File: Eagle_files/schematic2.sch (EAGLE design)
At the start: 76 parts, among them IC6 DS3231/SO

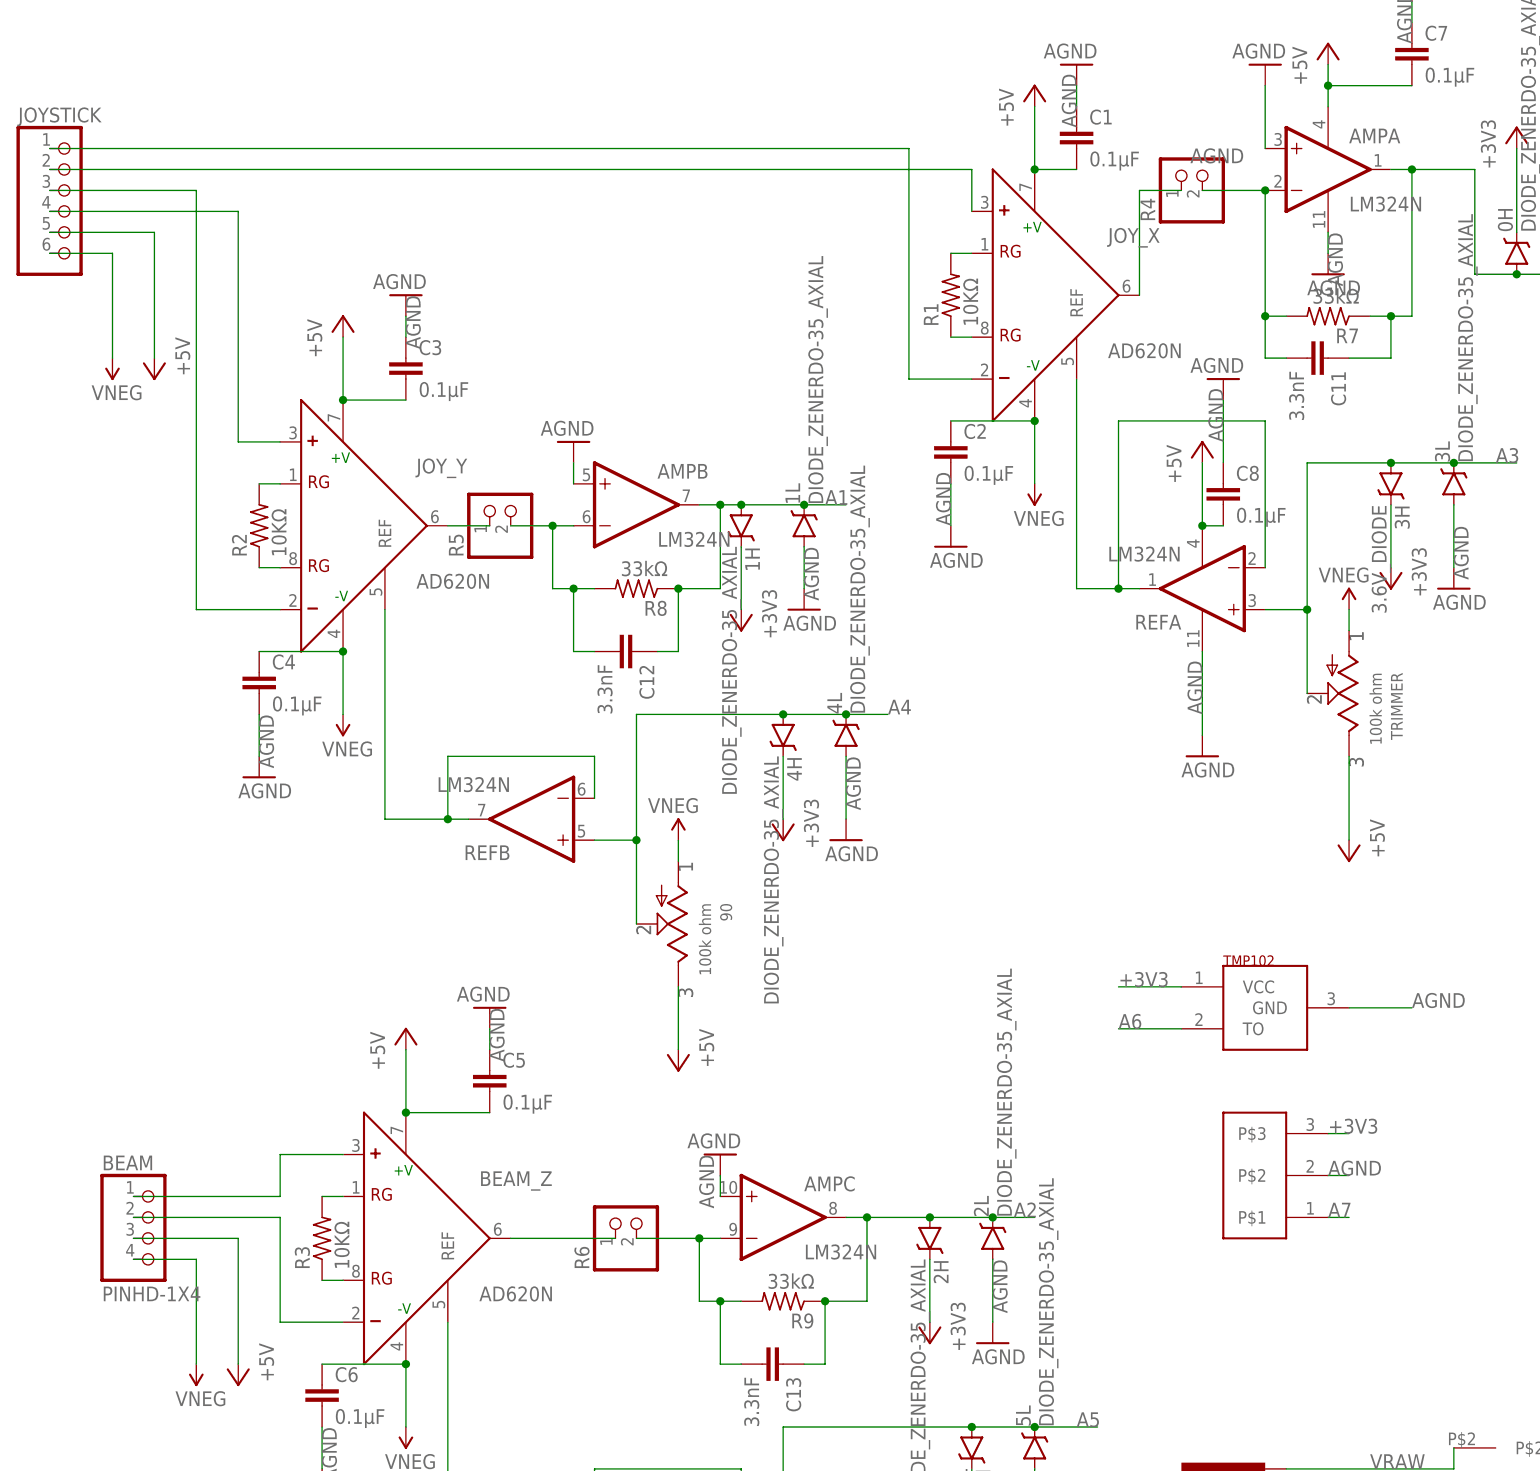
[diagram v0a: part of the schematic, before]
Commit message: Aligned all of the diodes to make a little more room. Increased the spacing between the analog ground plane and the neighboring planes. Rewired the A7 analog header so it conforms to standard TMP35, LM35 style temperature sensor pinouts. Swapped the gain-setting resistors on the In-AMPS to 2-pin header style so that we can swap resistors easily to change gain.
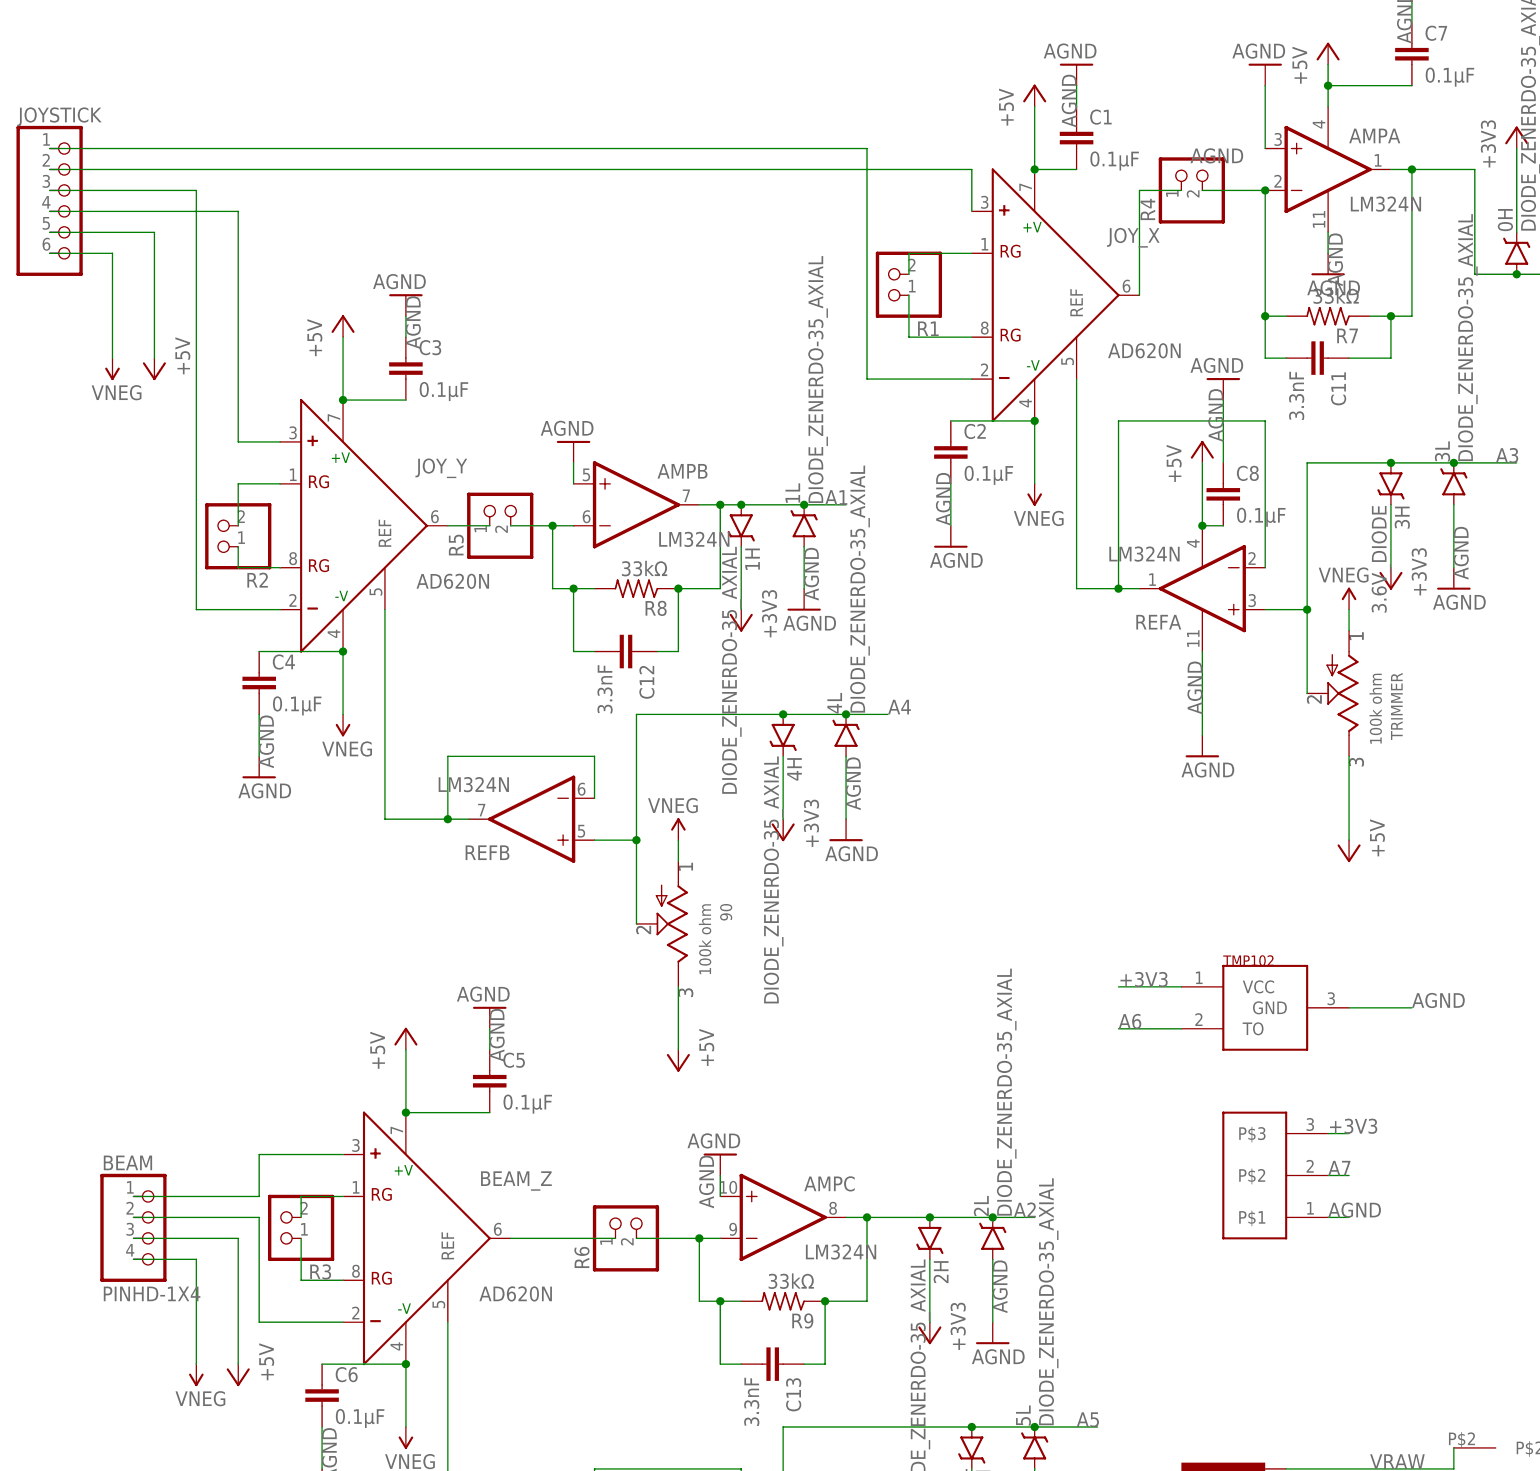
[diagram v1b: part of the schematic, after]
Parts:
- R1, R2, R3: value 10KΩ -> (none); device Felicia_force_logger:RESISTOR_SMDR0805 -> Felicia_force_logger:PINHD-1X2
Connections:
- net A7: now also ANALOG7_HEADER.P$2; no longer ANALOG7_HEADER.P$1
- net AGND: now also ANALOG7_HEADER.P$1; no longer ANALOG7_HEADER.P$2
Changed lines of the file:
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@@
 <part name="C12" library="Felicia_force_logger" deviceset="CAP" device="0805" value="3.3nF"/>
 <part name="C11" library="Felicia_force_logger" deviceset="CAP" device="0805" value="3.3nF"/>
-<part name="R2" library="Felicia_force_logger" deviceset="RESISTOR_SMD" device="R0805" value="10KΩ"/>
-<part name="R1" library="Felicia_force_logger" deviceset="RESISTOR_SMD" device="R0805" value="10KΩ"/>
-<part name="R3" library="Felicia_force_logger" deviceset="RESISTOR_SMD" device="R0805" value="10KΩ"/>
 <part name="U$3" library="Felicia_force_logger" deviceset="DC-DC_CONVERTER_DUAL_SUPPLY" device=""/>
 <part name="GND7" library="Felicia_force_logger" deviceset="GND" device=""/>
@@
 <part name="STANDOFF2" library="miller" deviceset="STAND-OFF" device=""/>
 <part name="I2C_HEADER" library="Felicia_force_logger" deviceset="PINHD-1X6" device="LOCK"/>
+<part name="R2" library="Felicia_force_logger" deviceset="PINHD-1X2" device=""/>
+<part name="R1" library="Felicia_force_logger" deviceset="PINHD-1X2" device=""/>
+<part name="R3" library="Felicia_force_logger" deviceset="PINHD-1X2" device=""/>
 </parts>
 <sheets>
@@
 <instance part="C12" gate="G$1" x="66.04" y="139.7" rot="R270"/>
 <instance part="C11" gate="G$1" x="149.86" y="175.26" rot="R270"/>
-<instance part="R2" gate="G$1" x="22.86" y="154.94" rot="R90"/>
-<instance part="R1" gate="G$1" x="106.68" y="182.88" rot="R90"/>
-<instance part="R3" gate="G$1" x="30.48" y="68.58" rot="R90"/>
 <instance part="U$3" gate="G$1" x="170.18" y="15.24"/>
 <instance part="GND7" gate="1" x="147.32" y="7.62"/>
@@
 <instance part="STANDOFF2" gate="G$1" x="12.7" y="5.08"/>
 <instance part="I2C_HEADER" gate="A" x="314.96" y="160.02"/>
+<instance part="R2" gate="G$1" x="17.78" y="154.94" rot="R180"/>
+<instance part="R1" gate="G$1" x="99.06" y="185.42" rot="R180"/>
+<instance part="R3" gate="G$1" x="25.4" y="71.12" rot="R180"/>
 </instances>
 <busses>
@@
 <segment>
 <pinref part="JOY_X" gate="G$1" pin="RG@1"/>
-<wire x1="106.68" y1="187.96" x2="109.22" y2="187.96" width="0.1524" layer="91"/>
 <pinref part="R1" gate="G$1" pin="2"/>
+<wire x1="109.22" y1="187.96" x2="101.6" y2="187.96" width="0.1524" layer="91"/>
+<wire x1="101.6" y1="187.96" x2="101.6" y2="185.42" width="0.1524" layer="91"/>
 </segment>
 </net>
@@
 <segment>
 <pinref part="JOY_X" gate="G$1" pin="RG@2"/>
-<wire x1="106.68" y1="177.8" x2="109.22" y2="177.8" width="0.1524" layer="91"/>
 <pinref part="R1" gate="G$1" pin="1"/>
+<wire x1="109.22" y1="177.8" x2="101.6" y2="177.8" width="0.1524" layer="91"/>
+<wire x1="101.6" y1="177.8" x2="101.6" y2="182.88" width="0.1524" layer="91"/>
 </segment>
 </net>
@@
 <segment>
 <pinref part="BEAM_Z" gate="G$1" pin="RG@1"/>
-<wire x1="30.48" y1="73.66" x2="33.02" y2="73.66" width="0.1524" layer="91"/>
 <pinref part="R3" gate="G$1" pin="2"/>
+<wire x1="33.02" y1="73.66" x2="27.94" y2="73.66" width="0.1524" layer="91"/>
+<wire x1="27.94" y1="73.66" x2="27.94" y2="71.12" width="0.1524" layer="91"/>
 </segment>
 </net>
@@
 <segment>
 <pinref part="BEAM_Z" gate="G$1" pin="RG@2"/>
-<wire x1="30.48" y1="63.5" x2="33.02" y2="63.5" width="0.1524" layer="91"/>
 <pinref part="R3" gate="G$1" pin="1"/>
+<wire x1="33.02" y1="63.5" x2="27.94" y2="63.5" width="0.1524" layer="91"/>
+<wire x1="27.94" y1="63.5" x2="27.94" y2="68.58" width="0.1524" layer="91"/>
 </segment>
 </net>
@@
 <net name="N$19" class="0">
 <segment>
-<wire x1="101.6" y1="200.66" x2="101.6" y2="172.72" width="0.1524" layer="91"/>
+<wire x1="96.52" y1="200.66" x2="96.52" y2="172.72" width="0.1524" layer="91"/>
 <pinref part="JOY_X" gate="G$1" pin="-"/>
-<wire x1="101.6" y1="172.72" x2="109.22" y2="172.72" width="0.1524" layer="91"/>
+<wire x1="96.52" y1="172.72" x2="109.22" y2="172.72" width="0.1524" layer="91"/>
 <pinref part="JOYSTICK" gate="A" pin="1"/>
-<wire x1="-2.54" y1="200.66" x2="101.6" y2="200.66" width="0.1524" layer="91"/>
+<wire x1="-2.54" y1="200.66" x2="96.52" y2="200.66" width="0.1524" layer="91"/>
 </segment>
 </net>
@@
 <pinref part="JOY_Y" gate="G$1" pin="RG@1"/>
 <pinref part="R2" gate="G$1" pin="2"/>
-<wire x1="22.86" y1="160.02" x2="25.4" y2="160.02" width="0.1524" layer="91"/>
+<wire x1="25.4" y1="160.02" x2="20.32" y2="160.02" width="0.1524" layer="91"/>
+<wire x1="20.32" y1="160.02" x2="20.32" y2="154.94" width="0.1524" layer="91"/>
 </segment>
 </net>
@@
 <pinref part="JOY_Y" gate="G$1" pin="RG@2"/>
 <pinref part="R2" gate="G$1" pin="1"/>
-<wire x1="22.86" y1="149.86" x2="25.4" y2="149.86" width="0.1524" layer="91"/>
+<wire x1="25.4" y1="149.86" x2="20.32" y2="149.86" width="0.1524" layer="91"/>
+<wire x1="20.32" y1="149.86" x2="20.32" y2="152.4" width="0.1524" layer="91"/>
 </segment>
 </net>
@@
 <segment>
 <pinref part="BEAM" gate="G$1" pin="2"/>
-<wire x1="7.62" y1="71.12" x2="25.4" y2="71.12" width="0.1524" layer="91"/>
-<wire x1="25.4" y1="71.12" x2="25.4" y2="58.42" width="0.1524" layer="91"/>
+<wire x1="7.62" y1="71.12" x2="22.86" y2="71.12" width="0.1524" layer="91"/>
+<wire x1="22.86" y1="71.12" x2="22.86" y2="58.42" width="0.1524" layer="91"/>
 <pinref part="BEAM_Z" gate="G$1" pin="-"/>
-<wire x1="25.4" y1="58.42" x2="33.02" y2="58.42" width="0.1524" layer="91"/>
+<wire x1="22.86" y1="58.42" x2="33.02" y2="58.42" width="0.1524" layer="91"/>
 </segment>
 </net>
@@
 <segment>
 <pinref part="BEAM" gate="G$1" pin="1"/>
-<wire x1="7.62" y1="73.66" x2="25.4" y2="73.66" width="0.1524" layer="91"/>
-<wire x1="25.4" y1="73.66" x2="25.4" y2="78.74" width="0.1524" layer="91"/>
+<wire x1="7.62" y1="73.66" x2="22.86" y2="73.66" width="0.1524" layer="91"/>
+<wire x1="22.86" y1="73.66" x2="22.86" y2="78.74" width="0.1524" layer="91"/>
 <pinref part="BEAM_Z" gate="G$1" pin="+"/>
-<wire x1="25.4" y1="78.74" x2="33.02" y2="78.74" width="0.1524" layer="91"/>
+<wire x1="22.86" y1="78.74" x2="33.02" y2="78.74" width="0.1524" layer="91"/>
 </segment>
 </net>
@@
 </segment>
 <segment>
-<pinref part="ANALOG7_HEADER" gate="G$1" pin="P$1"/>
-<wire x1="152.4" y1="71.12" x2="154.94" y2="71.12" width="0.1524" layer="91"/>
-<label x="152.4" y="71.12" size="1.778" layer="95"/>
+<pinref part="ANALOG7_HEADER" gate="G$1" pin="P$2"/>
+<wire x1="152.4" y1="76.2" x2="154.94" y2="76.2" width="0.1524" layer="91"/>
+<label x="152.4" y="76.2" size="1.778" layer="95"/>
 </segment>
 </net>
@@
 </net>
 <net name="AGND" class="0">
-<segment>
-<pinref part="ANALOG7_HEADER" gate="G$1" pin="P$2"/>
-<wire x1="152.4" y1="76.2" x2="154.94" y2="76.2" width="0.1524" layer="91"/>
-<label x="152.4" y="76.2" size="1.778" layer="95"/>
-</segment>
 <segment>
 <pinref part="0L" gate="G$1" pin="A"/>
@@
 <label x="22.86" y="132.08" size="1.778" layer="95" rot="R270"/>
 </segment>
-</net>
+<segment>
+<pinref part="ANALOG7_HEADER" gate="G$1" pin="P$1"/>
+<wire x1="152.4" y1="71.12" x2="154.94" y2="71.12" width="0.1524" layer="91"/>
+<label x="152.4" y="71.12" size="1.778" layer="95"/>
+</segment>
+</net>
